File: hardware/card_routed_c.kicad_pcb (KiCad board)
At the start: 2 copper layers, 143 x 80 mm, 1 part

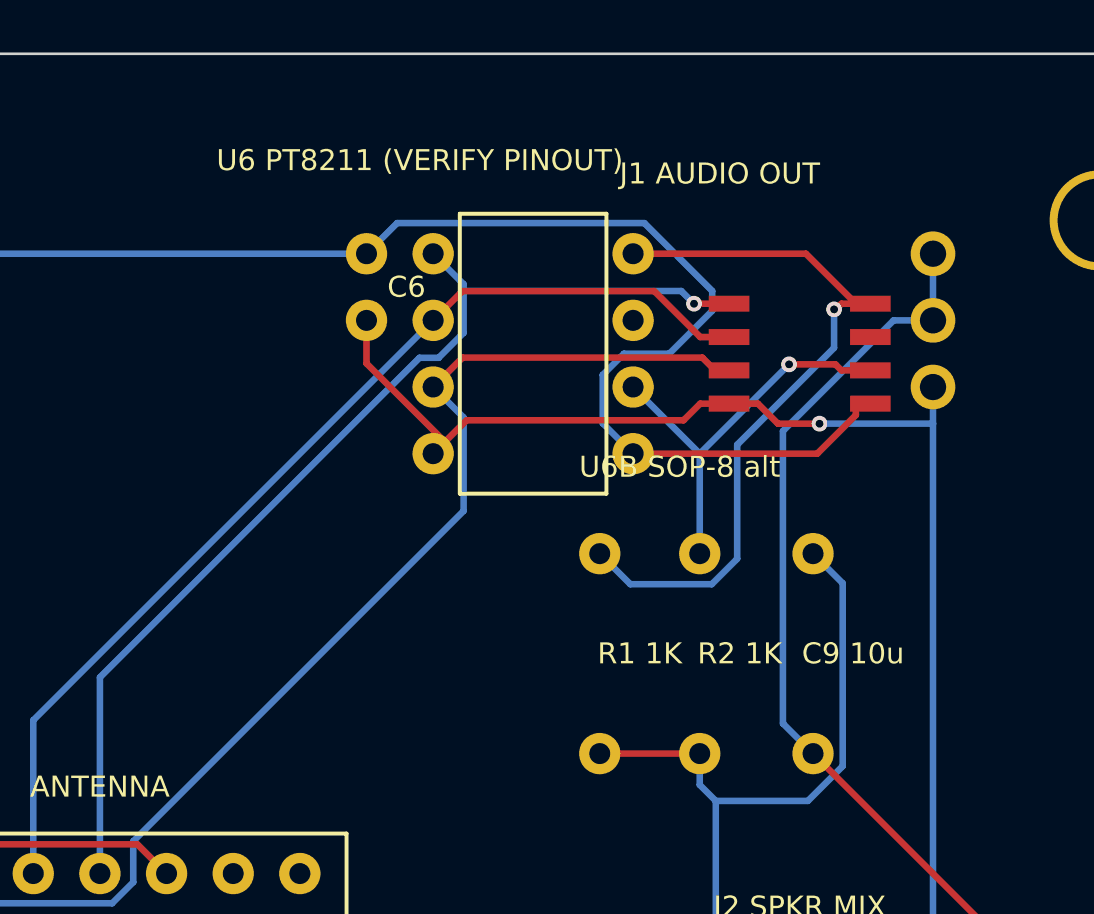
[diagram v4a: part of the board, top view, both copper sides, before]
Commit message: PT8211 datasheet in-tree; pinout verified and corrected
PT8211-S.pdf (Princeton Technology, v1.1) added to hardware/. The
flagged from-memory pinout was right on 6 of 8 pins: 6/8 were L/R
swapped (harmless — both sum to mono) and are now labeled truthfully
(6=LCH, 8=RCH, 7=NC). Datasheet also confirms both packages exist
(PT8211 DIP-8 / PT8211-S SO-8, matching our dual position) and that
the serial format is Japanese/LSB-justified, NOT standard I2S — noted
as a firmware requirement. 3.3V operation noted as Pico-ecosystem
practice vs the 5V nominal. Re-routed, DRC 0/0; fab package
regenerated. The last pre-order human check is closed.

Co-Authored-By: Claude Fable 5 <noreply@anthropic.com>
Claude-Session: https://claude.ai/code/session_01PB6zhL6oFB9zbtD4W85UDt
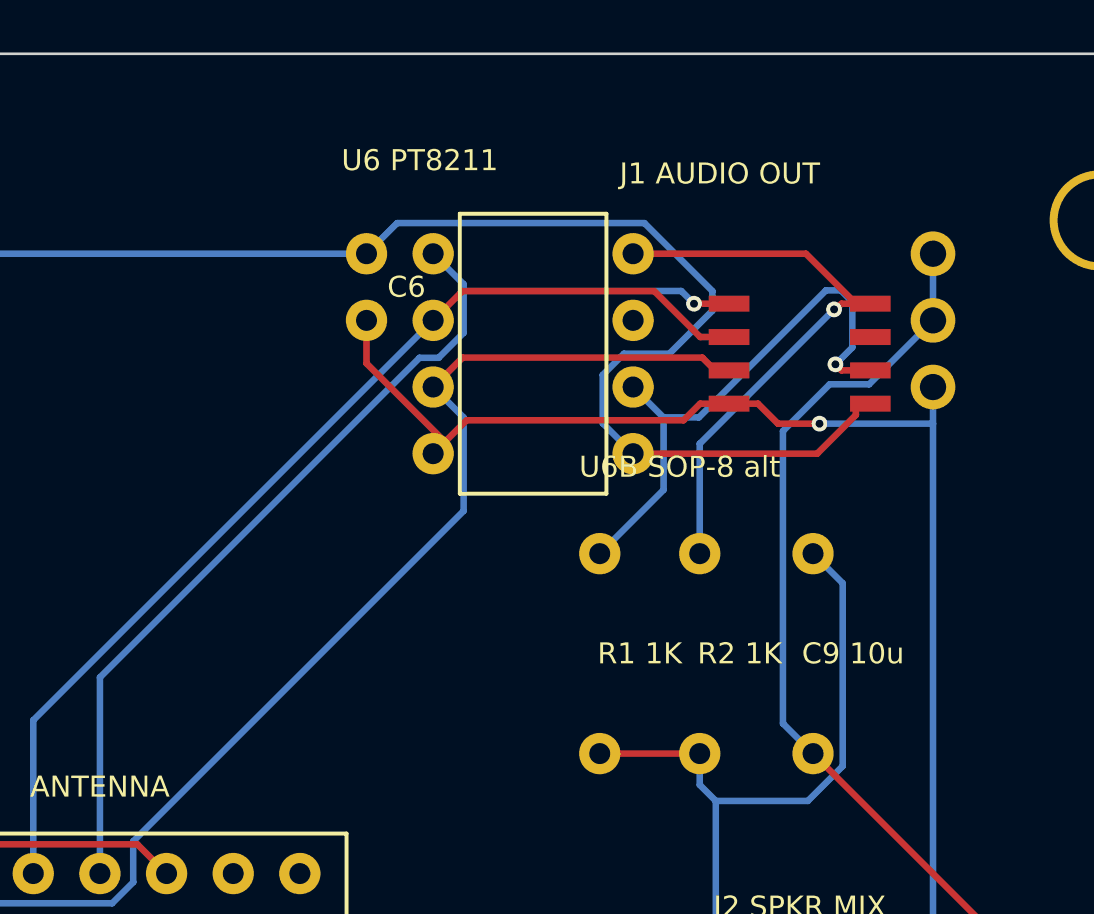
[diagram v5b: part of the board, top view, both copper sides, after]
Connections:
- ? pad 122: AOL -> AOR
- ? pad 126: AOR -> AOL
- ? pad 130: AOL -> AOR
- ? pad 134: AOR -> AOL
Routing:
- net AOR: track 15.4 -> 22.2 mm
- net AOL: track 27.9 -> 21.3 mm
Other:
- board text added: "U6 PT8211"
- board text removed: "U6 PT8211 (VERIFY PINOUT)"

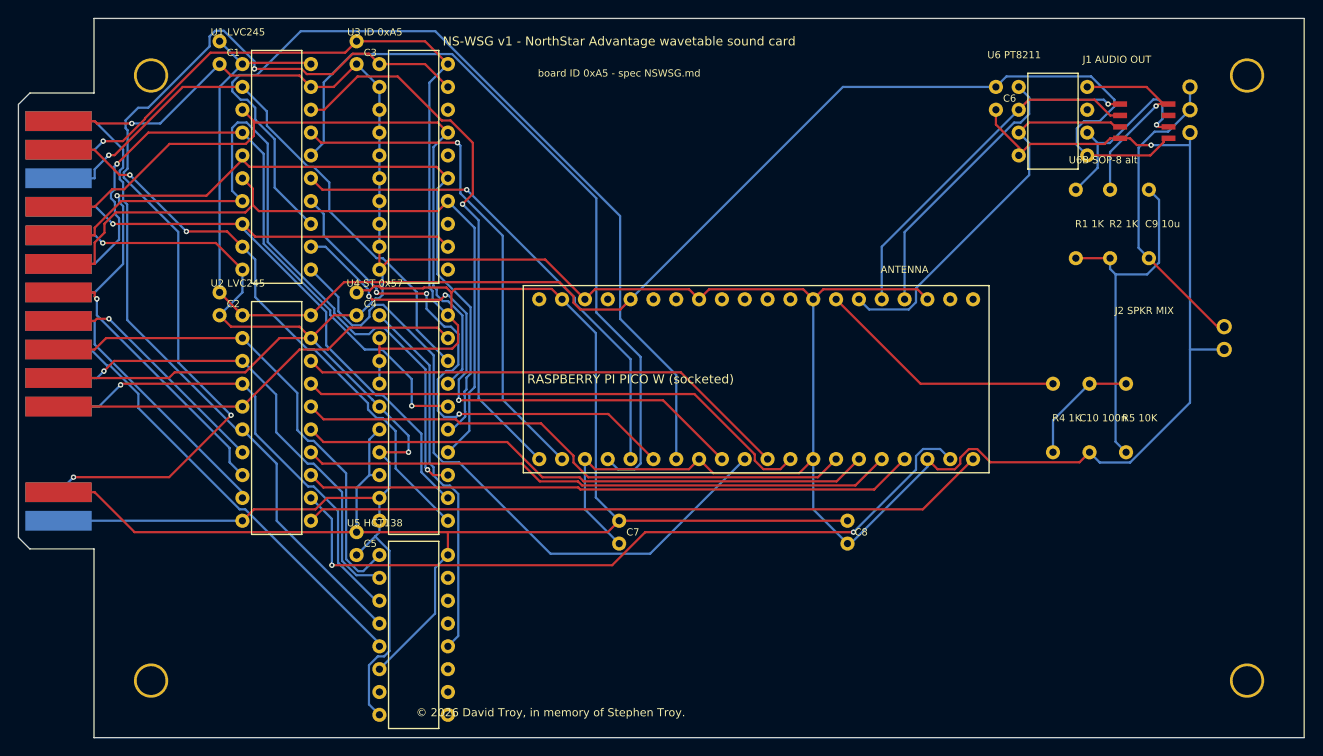
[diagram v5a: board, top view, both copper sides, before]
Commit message: On-board 3.5mm jack, stereo output per the PJRC PT8211 topology
Adopted the protosupplies/PJRC PT8211 adapter design: LCH/RCH each
through 47uF coupling to a real CUI SJ1-3523N TRS jack (footprint
taken from the KiCad-maintained library, rotated so the barrel
overhangs the right board edge) — true stereo replaces the mono sum,
so firmware can pan voices. VDD gets the datasheet's 10R + 47u + 100n
filter (new VDDF rail). PWM fallback and J2 mix-in re-plumbed to the
left channel. Fixed import_ses.py dropping wires for quoted net names
(underscored nets like AOL_C). Re-routed, DRC 0/0, fab package and
docs regenerated.

Co-Authored-By: Claude Fable 5 <noreply@anthropic.com>
Claude-Session: https://claude.ai/code/session_01PB6zhL6oFB9zbtD4W85UDt
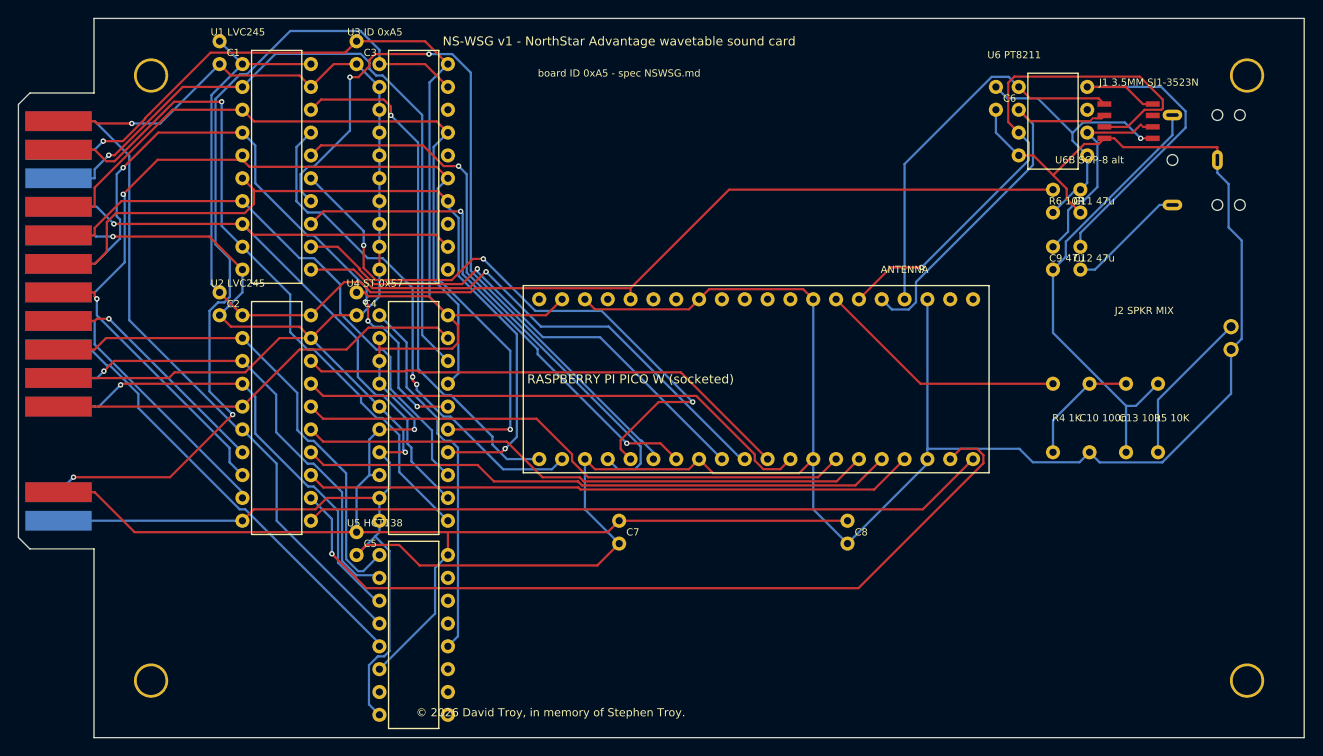
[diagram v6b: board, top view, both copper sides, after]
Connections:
- ? pad 122: AOR -> RCH
- ? pad 126: AOL -> LCH
- ? pad 128: +3V3 -> VDDF
- ? pad 130: AOR -> RCH
- ? pad 134: AOL -> LCH
- ? pad 136: +3V3 -> VDDF
- ? pad 177: AOL -> +3V3
- ? pad 178: ASUM -> VDDF
- ? pad 179: AOR -> VDDF
- ? pad 180: ASUM -> GND
- ? pad 181: ASUM -> LCH
- ? pad 182: AOUT -> AOL_C
- ? pad 183: PWM -> RCH
- ? pad 184: PWMF -> AOR_C
- ? pad 185: PWMF -> PWM
- ? pad 186: GND -> PWMF
- ? pad 188: ASUM -> GND
- ? pad 189: AOUT -> PWMF
- ? pad 190: AOUT -> AOL_C
- ? pad 191: GND -> AOL_C
- ? pad 192: AOUT -> J2SIG
- ? pad 193: GND -> (no net)
- ? pad 194: +3V3 -> (no net)
- ? pad 195: GND -> (no net)
- ? pad 196: +3V3 -> (no net)
- ? pad 197: GND -> (no net)
- ? pad 198: +5V -> J2SIG
- ? pad 200: +5V -> +3V3
- ? pad 202: +5V -> +3V3
- ? pad 204: +3V3 -> +5V
- ? pad 210: (no net) -> VDDF
- ? pad 211: (no net) -> GND
- ? pad 212: (no net) -> +5V
- ? pad 213: (no net) -> GND
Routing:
- net AOL_C: track 0.00 -> 51.0 mm
- net GP5: track 103.4 -> 56.9 mm, vias 0 -> 2
- net ASUM: track 40.1 -> 0.00 mm
- net RCH: track 0.00 -> 40.1 mm
- net AOUT: track 34.3 -> 0.00 mm
- net +3V3: track 172.9 -> 140.1 mm
- net VDDF: track 0.00 -> 32.2 mm, vias 0 -> 1
- net LCH: track 0.00 -> 23.4 mm
- net GP4: track 61.5 -> 84.2 mm, vias 3 -> 2
- net AOR: track 22.2 -> 0.00 mm, vias 1 -> 0
- net IO5: track 85.3 -> 63.8 mm, vias 1 -> 0
- net AOL: track 21.3 -> 0.00 mm, vias 1 -> 0
- net GP2: track 82.9 -> 63.7 mm, vias 0 -> 1
- net +5V: track 272.9 -> 254.1 mm, vias 1 -> 2
- net GND: track 479.0 -> 497.6 mm, vias 4 -> 3
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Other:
- board text added: "C11 47u"
- board text added: "C12 47u"
- board text added: "C13 10u"
- board text added: "C9 47u"
- board text added: "J1 3.5MM SJ1-3523N"
- board text added: "R6 10R"
- board text removed: "C9 10u"
- board text removed: "J1 AUDIO OUT"
- board text removed: "R1 1K"
- board text removed: "R2 1K"

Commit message: Silkscreen tidy: zero collisions at full DRC severity
Root cause was gr_text center-anchoring vs left-anchored placement
assumptions. DIP references now run vertically inside their body
outlines (collision-proof), audio passives use short staggered refs
(values in the BOM), Pico label centered within its outline, memorial
line shifted clear of U5. Full-severity DRC is down from 13 findings
to just the benign embedded-footprint-library notice. Fab package and
plots regenerated.

Co-Authored-By: Claude Fable 5 <noreply@anthropic.com>
Claude-Session: https://claude.ai/code/session_01PB6zhL6oFB9zbtD4W85UDt
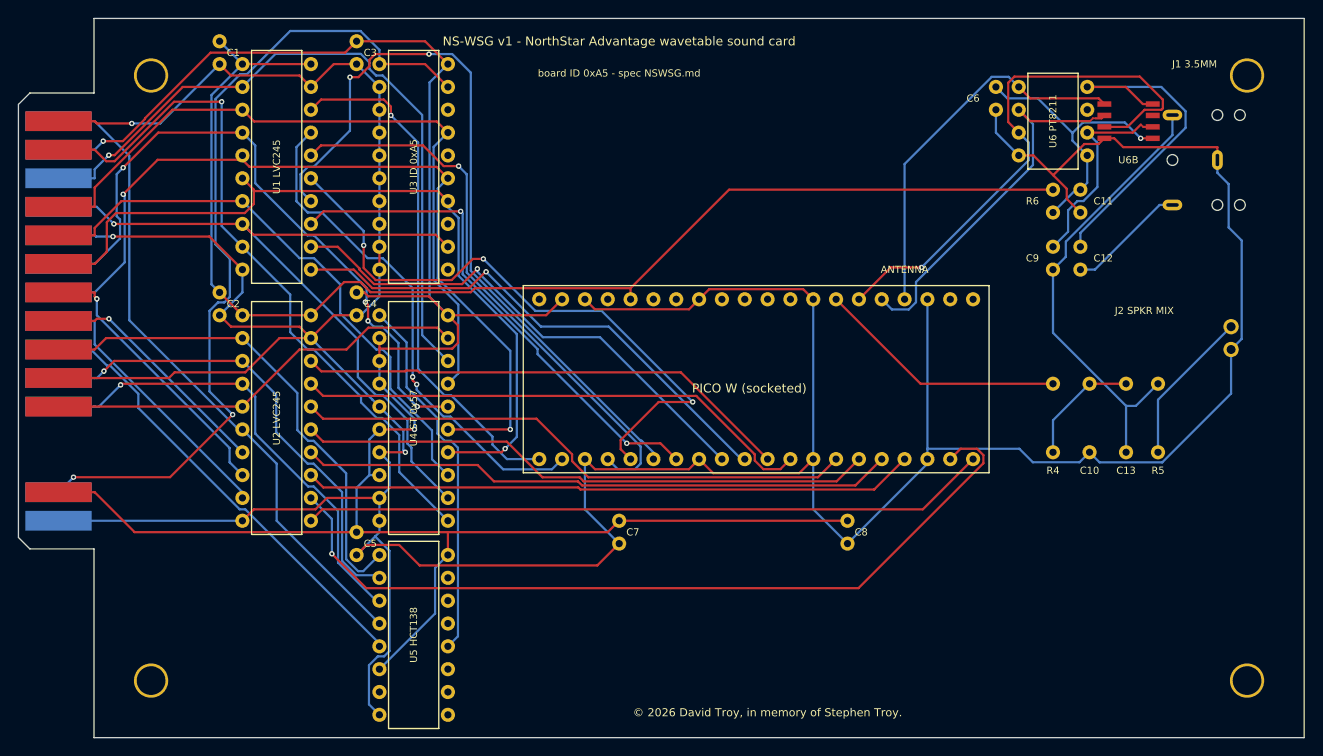
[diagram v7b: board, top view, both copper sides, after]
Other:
- board text added: "C10"
- board text added: "C11"
- board text added: "C12"
- board text added: "C13"
- board text added: "C9"
- board text added: "J1 3.5MM"
- board text added: "PICO W (socketed)"
- board text added: "R4"
- board text added: "R5"
- board text added: "R6"
- board text added: "U6B"
- board text removed: "C10 100n"
- board text removed: "C11 47u"
- board text removed: "C12 47u"
- board text removed: "C13 10u"
- board text removed: "C9 47u"
- board text removed: "J1 3.5MM SJ1-3523N"
- board text removed: "R4 1K"
- board text removed: "R5 10K"
- board text removed: "R6 10R"
- board text removed: "RASPBERRY PI PICO W (socketed)"
- board text removed: "U6B SOP-8 alt"
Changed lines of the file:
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@@
   (gr_line (start 85.0000 73.2982) (end 85.0000 65.0000) (layer "Edge.Cuts") (width 0.1))
   (gr_rect (start 102.5260 68.5560) (end 108.1140 94.4640) (layer "F.SilkS") (width 0.15) (fill none))
-  (gr_text "U1 LVC245" (at 101.0020 66.5240) (layer "F.SilkS") (effects (font (size 0.8 0.8) (thickness 0.15))))
+  (gr_text "U1 LVC245" (at 105.3200 81.5100 90) (layer "F.SilkS") (effects (font (size 0.8 0.8) (thickness 0.15))))
   (gr_rect (start 102.5260 96.4960) (end 108.1140 122.4040) (layer "F.SilkS") (width 0.15) (fill none))
-  (gr_text "U2 LVC245" (at 101.0020 94.4640) (layer "F.SilkS") (effects (font (size 0.8 0.8) (thickness 0.15))))
+  (gr_text "U2 LVC245" (at 105.3200 109.4500 90) (layer "F.SilkS") (effects (font (size 0.8 0.8) (thickness 0.15))))
   (gr_rect (start 117.7660 68.5560) (end 123.3540 94.4640) (layer "F.SilkS") (width 0.15) (fill none))
-  (gr_text "U3 ID 0xA5" (at 116.2420 66.5240) (layer "F.SilkS") (effects (font (size 0.8 0.8) (thickness 0.15))))
+  (gr_text "U3 ID 0xA5" (at 120.5600 81.5100 90) (layer "F.SilkS") (effects (font (size 0.8 0.8) (thickness 0.15))))
   (gr_rect (start 117.7660 96.4960) (end 123.3540 122.4040) (layer "F.SilkS") (width 0.15) (fill none))
-  (gr_text "U4 ST 0x57" (at 116.2420 94.4640) (layer "F.SilkS") (effects (font (size 0.8 0.8) (thickness 0.15))))
+  (gr_text "U4 ST 0x57" (at 120.5600 109.4500 90) (layer "F.SilkS") (effects (font (size 0.8 0.8) (thickness 0.15))))
   (gr_rect (start 117.7660 123.1660) (end 123.3540 143.9940) (layer "F.SilkS") (width 0.15) (fill none))
-  (gr_text "U5 HCT138" (at 116.2420 121.1340) (layer "F.SilkS") (effects (font (size 0.8 0.8) (thickness 0.15))))
+  (gr_text "U5 HCT138" (at 120.5600 133.5800 90) (layer "F.SilkS") (effects (font (size 0.8 0.8) (thickness 0.15))))
   (gr_rect (start 188.8860 71.0960) (end 194.4740 81.7640) (layer "F.SilkS") (width 0.15) (fill none))
-  (gr_text "U6 PT8211" (at 187.3620 69.0640) (layer "F.SilkS") (effects (font (size 0.8 0.8) (thickness 0.15))))
-  (gr_text "U6B SOP-8 alt" (at 195.7440 80.7480) (layer "F.SilkS") (effects (font (size 0.8 0.8) (thickness 0.15))))
+  (gr_text "U6 PT8211" (at 191.6800 76.4300 90) (layer "F.SilkS") (effects (font (size 0.8 0.8) (thickness 0.15))))
+  (gr_text "U6B" (at 200.0620 80.7480) (layer "F.SilkS") (effects (font (size 0.8 0.8) (thickness 0.15))))
   (gr_rect (start 132.7520 94.7180) (end 184.5680 115.5460) (layer "F.SilkS") (width 0.15) (fill none))
-  (gr_text "RASPBERRY PI PICO W (socketed)" (at 144.6900 105.1320) (layer "F.SilkS") (effects (font (size 1.0 1.0) (thickness 0.15))))
+  (gr_text "PICO W (socketed)" (at 157.8980 106.1480) (layer "F.SilkS") (effects (font (size 1.0 1.0) (thickness 0.15))))
   (gr_text "ANTENNA" (at 175.1700 92.9400) (layer "F.SilkS") (effects (font (size 0.8 0.8) (thickness 0.15))))
   (zone (net 0) (net_name "") (layers "F.Cu" "B.Cu") (name "antenna-keepout") (hatch edge 0.508) (connect_pads (clearance 0)) (min_thickness 0.25) (keepout (tracks allowed) (vias not_allowed) (pads allowed) (copperpour not_allowed) (footprints allowed)) (fill (thermal_gap 0.5) (thermal_bridge_width 0.5)) (polygon (pts (xy 91.948 28.956) (xy 102.108 28.956) (xy 102.108 51.308) (xy 91.948 51.308))))
-  (gr_text "R6 10R" (at 193.2040 85.3200) (layer "F.SilkS") (effects (font (size 0.8 0.8) (thickness 0.15))))
-  (gr_text "C11 47u" (at 196.2520 85.3200) (layer "F.SilkS") (effects (font (size 0.8 0.8) (thickness 0.15))))
-  (gr_text "C9 47u" (at 193.2040 91.6700) (layer "F.SilkS") (effects (font (size 0.8 0.8) (thickness 0.15))))
-  (gr_text "C12 47u" (at 196.2520 91.6700) (layer "F.SilkS") (effects (font (size 0.8 0.8) (thickness 0.15))))
-  (gr_text "R4 1K" (at 193.2040 109.4500) (layer "F.SilkS") (effects (font (size 0.8 0.8) (thickness 0.15))))
-  (gr_text "C10 100n" (at 197.2680 109.4500) (layer "F.SilkS") (effects (font (size 0.8 0.8) (thickness 0.15))))
-  (gr_text "C13 10u" (at 201.3320 109.4500) (layer "F.SilkS") (effects (font (size 0.8 0.8) (thickness 0.15))))
-  (gr_text "R5 10K" (at 204.8880 109.4500) (layer "F.SilkS") (effects (font (size 0.8 0.8) (thickness 0.15))))
-  (gr_text "J1 3.5MM SJ1-3523N" (at 202.3480 72.1120) (layer "F.SilkS") (effects (font (size 0.8 0.8) (thickness 0.15))))
+  (gr_text "R6" (at 189.3940 85.3200) (layer "F.SilkS") (effects (font (size 0.8 0.8) (thickness 0.15))))
+  (gr_text "C11" (at 197.2680 85.3200) (layer "F.SilkS") (effects (font (size 0.8 0.8) (thickness 0.15))))
+  (gr_text "C9" (at 189.3940 91.6700) (layer "F.SilkS") (effects (font (size 0.8 0.8) (thickness 0.15))))
+  (gr_text "C12" (at 197.2680 91.6700) (layer "F.SilkS") (effects (font (size 0.8 0.8) (thickness 0.15))))
+  (gr_text "R4" (at 191.6800 115.2920) (layer "F.SilkS") (effects (font (size 0.8 0.8) (thickness 0.15))))
+  (gr_text "C10" (at 195.7440 115.2920) (layer "F.SilkS") (effects (font (size 0.8 0.8) (thickness 0.15))))
+  (gr_text "C13" (at 199.8080 115.2920) (layer "F.SilkS") (effects (font (size 0.8 0.8) (thickness 0.15))))
+  (gr_text "R5" (at 203.3640 115.2920) (layer "F.SilkS") (effects (font (size 0.8 0.8) (thickness 0.15))))
+  (gr_text "J1 3.5MM" (at 207.4280 70.0800) (layer "F.SilkS") (effects (font (size 0.8 0.8) (thickness 0.15))))
   (gr_text "J2 SPKR MIX" (at 201.8400 97.5120) (layer "F.SilkS") (effects (font (size 0.8 0.8) (thickness 0.15))))
   (gr_text "C1" (at 100.4940 68.8100) (layer "F.SilkS") (effects (font (size 0.8 0.8) (thickness 0.15))))
@@
   (gr_text "C4" (at 115.7340 96.7500) (layer "F.SilkS") (effects (font (size 0.8 0.8) (thickness 0.15))))
   (gr_text "C5" (at 115.7340 123.4200) (layer "F.SilkS") (effects (font (size 0.8 0.8) (thickness 0.15))))
-  (gr_text "C6" (at 186.8540 73.8900) (layer "F.SilkS") (effects (font (size 0.8 0.8) (thickness 0.15))))
+  (gr_text "C6" (at 182.7900 73.8900) (layer "F.SilkS") (effects (font (size 0.8 0.8) (thickness 0.15))))
   (gr_text "C7" (at 144.9440 122.1500) (layer "F.SilkS") (effects (font (size 0.8 0.8) (thickness 0.15))))
   (gr_text "C8" (at 170.3440 122.1500) (layer "F.SilkS") (effects (font (size 0.8 0.8) (thickness 0.15))))
   (gr_text "NS-WSG v1 - NorthStar Advantage wavetable sound card" (at 143.4200 67.5400) (layer "F.SilkS") (effects (font (size 1.0 1.0) (thickness 0.15))))
   (gr_text "board ID 0xA5 - spec NSWSG.md" (at 143.4200 71.0960) (layer "F.SilkS") (effects (font (size 0.8 0.8) (thickness 0.15))))
-  (gr_text "© 2026 David Troy, in memory of Stephen Troy." (at 135.8000 142.2160) (layer "F.SilkS") (effects (font (size 0.9 0.9) (thickness 0.15))))
+  (gr_text "© 2026 David Troy, in memory of Stephen Troy." (at 159.9300 142.2160) (layer "F.SilkS") (effects (font (size 0.9 0.9) (thickness 0.15))))
   (segment (start 114.2100 70.0800) (end 111.6700 70.0800) (width 0.25) (layer "F.Cu") (net 1))
   (segment (start 111.6700 70.0800) (end 109.1300 72.6200) (width 0.25) (layer "F.Cu") (net 1))
